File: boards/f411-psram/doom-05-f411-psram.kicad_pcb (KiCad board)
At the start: 4 copper layers, 140 x 64 mm, 68 parts, among them J5 S2B-PH-K-S(LF)(SN), Q1 FS8205A, SW9 JS102011SAQN, U1 STM32F411CEU6, U2 APS6404L-3SQR-SN, U3 W25Q128JVSIQ, U4 TLV75533PDBVR, U5 MAX98357AETE+T, U6 TP4056, U7 DW01A, U8 ESD 2-line, Y1 25MHz 10pF

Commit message: PCBKit's mark and pcbkit.io on every board; the RP2350 handheld ready to order
The handheld runs from two 18650 cells in parallel behind a DW01A protector and a reverse-cell
P-MOSFET, charged at up to 500 mA from the Pico's USB-C by a BQ24075 (power path into VSYS, timers
off for 6 Ah), with an on/off switch on 3V3_EN, M3 holes, ground pours and the console on pads.
Every assembled part has a JLCPCB code in stock (Basic where there is one); the module sockets are
in the BOM, the modules listed in the order's README. Check complete, the ready review clean.
Every board: routed and checked complete with the new mark.
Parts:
- added logo: , Logo_PCBKit_pcbkit.io, F.Cu at (202.5, 194.8)
- SW1, SW2, SW3, SW4, SW5, SW6, SW7, SW8: value (none) -> PTS645SM43SMTR92 LFS
- SW10: value (none) -> TS-1187A-B-A-B

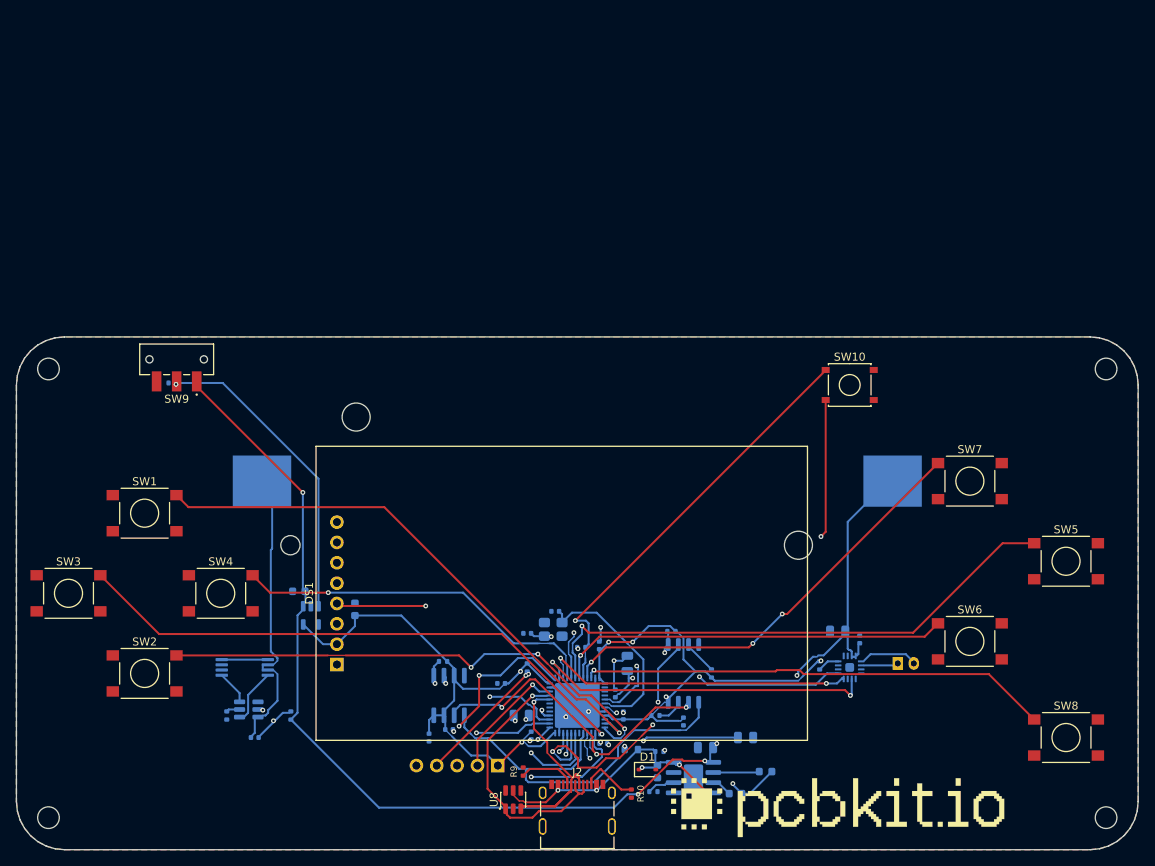
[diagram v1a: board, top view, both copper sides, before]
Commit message: f411-psram: two 18650 cells with protection and a USB-C charger; every part orderable
One 18650 with a TP4056 becomes two in parallel (Keystone 1042 holders on the back) behind a
reverse-cell P-FET and DW01A + FS8205A protection, charged by a BQ24075 with power path from the
USB-C (as boards/rp2350-handheld); the TLV75533 and the amplifier run from its SYS. A RESET button
beside BOOT for the ROM's USB DFU; the speaker connector on the right edge; menu moved to PB0 so
the decoupling at pin 48 leaves room to route. Board 140 x 104 mm, M3 holes, test pads; every
assembled part pinned to an LCSC code.
check: complete, 0 errors, 2 warnings (USB FS pair coupling and skew, justified in the README);
ready lens: nothing to fix; fab export without --force.

Claude-Session: https://claude.ai/code/session_01ATmMmxyrWxFwR3nTdXUrcx
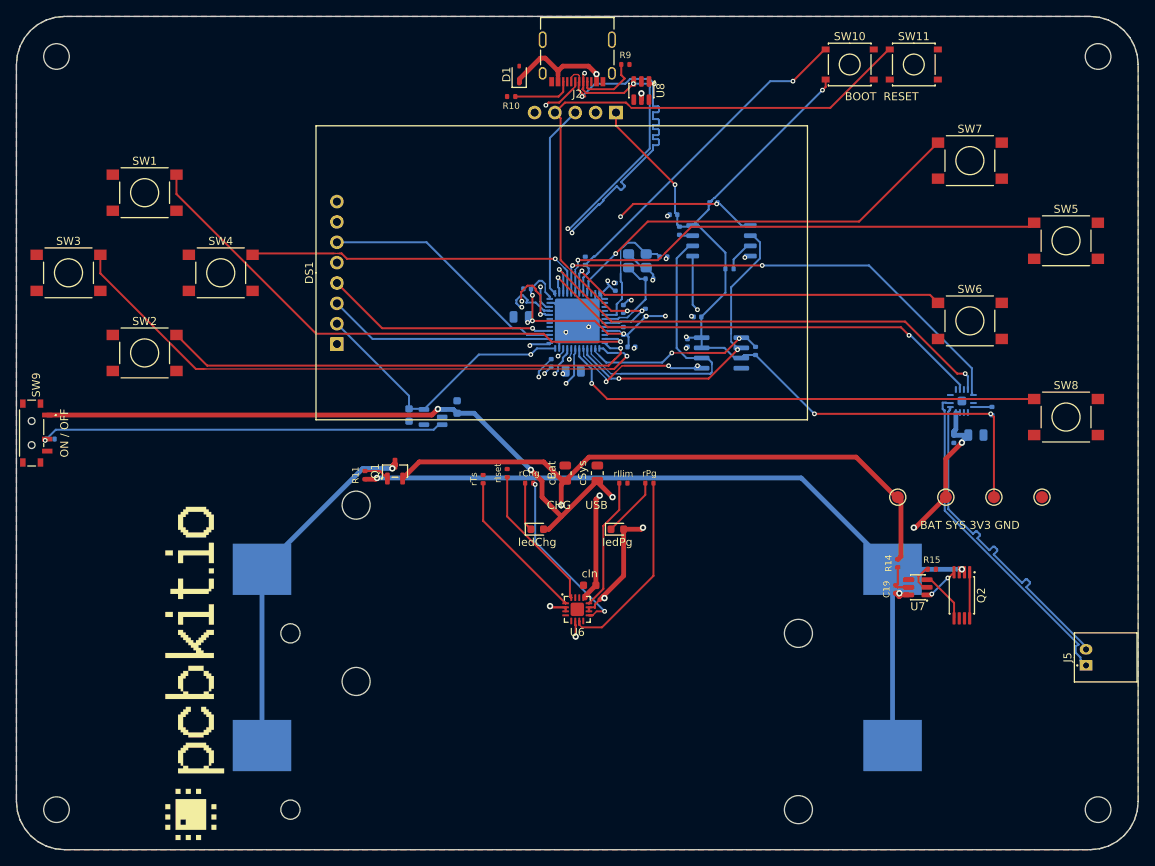
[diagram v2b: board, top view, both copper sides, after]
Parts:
- removed C17, C18: 10uF, C_0805_2012Metric
- removed C9: 1uF, C_0603_1608Metric
- removed D2: red, LED_0603_1608Metric
- removed D3: green, LED_0603_1608Metric
- removed R12: 1.2kohm, R_0402_1005Metric
- removed R13: 1kohm, R_0402_1005Metric
- added BT2: 1042, BatteryHolder_Keystone_1042_1x18650, B.Cu at (170.0, 165.0)
- added Q2: FS8205A, TSSOP-8_4.4x2.93mm_P0.65mm, F.Cu at (218.0, 168.2)
- added SW11: TS-1187A-B-A-B, SW_Tactile_SPST_5.1x5.1mm_SMD, F.Cu at (212.0, 102.0)
- added cBat: 4.7uF, C_0805_2012Metric, F.Cu at (168.5, 153.0)
- added cIn: 1uF, C_0603_1608Metric, F.Cu at (171.6, 167.0)
- added cSys: 4.7uF, C_0805_2012Metric, F.Cu at (172.5, 153.0)
- added ledChg: red, LED_0603_1608Metric, F.Cu at (165.0, 160.0)
- added ledPg: green, LED_0603_1608Metric, F.Cu at (175.0, 160.0)
- added rChg: 1.5kohm, R_0402_1005Metric, F.Cu at (164.0, 154.2)
- added rIlim: 1.18kohm, R_0402_1005Metric, F.Cu at (175.8, 154.2)
- added rIset: 1.13kohm, R_0402_1005Metric, F.Cu at (161.2, 153.0)
- added rPg: 1.5kohm, R_0402_1005Metric, F.Cu at (179.0, 154.2)
- added rTs: 10kohm, R_0402_1005Metric, F.Cu at (158.2, 153.8)
- added tpBat: , TestPoint_Round_D1.5mm, F.Cu at (210.0, 156.0)
- added tpGnd: , TestPoint_Round_D1.5mm, F.Cu at (228.0, 156.0)
- added tpSys: , TestPoint_Round_D1.5mm, F.Cu at (216.0, 156.0)
- added tpV3: , TestPoint_Round_D1.5mm, F.Cu at (222.0, 156.0)
- C19, J5, R14, R15, U7: moved to F.Cu
- H1, H2, H3, H4: footprint MountingHole_2.7mm_M2.5 -> MountingHole_3.2mm_M3
- Q1: value FS8205A -> AO3401A; footprint TSSOP-8_4.4x2.93mm_P0.65mm -> SOT-23; moved to F.Cu
- R11: value 1ohm -> 100kohm; footprint R_0603_1608Metric -> R_0402_1005Metric; moved to F.Cu
- SW9: value JS102011SAQN -> MSK12C02; footprint SW_Slide_SPDT_CK_JS102011SAQN_Horizontal -> SW_Slide_SPDT_Shouhan_MSK12C02
- U6: value TP4056 -> BQ24075RGTR; footprint SOIC-8-1EP_3.9x4.9mm_P1.27mm_EP2.413x3.302mm -> QFN-16-1EP_3x3mm_P0.5mm_EP1.68x1.68mm; moved to F.Cu
- moved U8 89.9 mm to (178.0, 105.2), turned to 270 degrees
- moved R15 89.9 mm to (214.2, 165.0), turned to 0 degrees
- moved R9 89.2 mm to (176.0, 102.0), turned to 0 degrees
- moved R10 88.3 mm to (161.8, 106.0), turned to 180 degrees
- moved D1 88.2 mm to (162.8, 103.2), turned to 90 degrees
- moved J2 87.7 mm to (170.0, 104.2), turned to 180 degrees
- moved U7 84.9 mm to (212.5, 167.2)
- moved J1 82.8 mm to (169.8, 108.0)
- moved C19 82.1 mm to (209.8, 167.5), turned to 90 degrees
- moved logo 82.0 mm to (122.2, 178.0), turned to 90 degrees
- moved R14 78.1 mm to (210.0, 164.2), turned to 90 degrees
- moved C14 63.3 mm to (182.0, 120.8), turned to 0 degrees
- moved R7 60.6 mm to (182.8, 122.8), turned to 90 degrees
- moved C13 60.1 mm to (185.0, 133.5), turned to 0 degrees
- moved C12 58.9 mm to (183.8, 136.8)
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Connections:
- net Net-(C7-1) renamed VCAP
- BT1 pad 1: VBAT -> CELL_N
- BT1 pad 2: BAT_N -> BAT_IN
- C15 pad 1: VBAT -> SYS
- C16 pad 1: VBAT -> SYS
- C19 pad 1: BAT_N -> CELL_N
- C20 pad 1: VBAT -> SYS
- Q1 pad 1: U7Support/DRAIN -> reversed/gate
- Q1 pad 2: BAT_N -> BAT
- Q1 pad 3: BAT_N -> BAT_IN
- R11 pad 1: VBUS -> CELL_N
- R11 pad 2: U6Support/C1_P -> reversed/gate
- R14 pad 1: VBAT -> Net-(C19-1)
- R14 pad 2: Net-(C19-1) -> BAT
- R5 pad 1: V3 -> ROM_CS
- R5 pad 2: ROM_CS -> V3
- SW9 pad 1: VBAT -> SYS
- U1 pad 18: (no net) -> MENU
- U1 pad 46: MENU -> (no net)
- U4 pad 1: VBAT -> SYS
- U5 pad 7: VBAT -> SYS
- U5 pad 8: VBAT -> SYS
- U6 pad 1: GND -> TS
- U6 pad 2: Net-(R12-1) -> BAT
- U6 pad 3: GND -> BAT
- U6 pad 4: VBUS -> GND
- U6 pad 5: VBAT -> GND
- U6 pad 6: Net-(D3-1) -> SYS
- U6 pad 7: Net-(D2-1) -> PG_N
- U6 pad 8: VBUS -> GND
- U6 pad 9: GND -> CHG_N
- U7 pad 1: Net-(Q1-4) -> Net-(Q2-4)
- U7 pad 3: Net-(Q1-5) -> Net-(Q2-5)
- U7 pad 6: BAT_N -> CELL_N
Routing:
- net SYS: track 0.00 -> 165.8 mm, vias 0 -> 8
- net VBAT: track 145.7 -> 0.00 mm, vias 5 -> 0
- net CELL_N: track 0.00 -> 104.5 mm, vias 0 -> 3
- net BAT: track 0.00 -> 94.0 mm, vias 0 -> 2
- net VBUS: track 36.1 -> 87.2 mm, vias 5 -> 3
- net NRST: track 35.6 -> 84.3 mm, vias 4 -> 2
- net BAT_IN: track 0.00 -> 47.3 mm, vias 0 -> 1
- net SPK_N: track 3.60 -> 41.7 mm
- net SPK_P: track 6.38 -> 41.3 mm
- net DP: track 31.0 -> 65.6 mm, vias 1 -> 4
- net DN: track 33.1 -> 66.4 mm, vias 1 -> 6
- net BAT_N: track 29.8 -> 0.00 mm
- net V3: track 185.6 -> 214.0 mm, vias 8 -> 14
- net PG_N: track 0.00 -> 25.0 mm
- net CHG_N: track 0.00 -> 22.5 mm, vias 0 -> 2
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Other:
- board size 140 x 64 mm -> 140 x 104 mm
- board text added: "+"
- board text added: "-"
- board text added: "2 x 18650 Li-ion 3.7 V"
- board text added: "BAT SYS 3V3 GND"
- board text added: "BOOT RESET"
- board text added: "CHG USB"
- board text added: "ON / OFF"
